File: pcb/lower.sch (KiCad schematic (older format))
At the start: 42 parts, among them J1 MALE, J10 TC2030_NL, J11 STANDOFF, J12 STANDOFF, J13 STANDOFF, J14 STANDOFF, J2 FEMALE, J3 MALE, J4 FEMALE, J5 MALE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

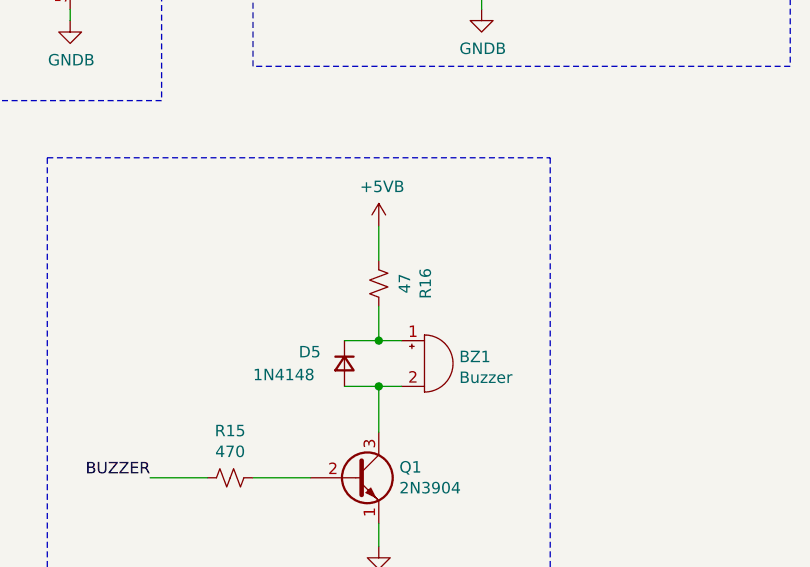
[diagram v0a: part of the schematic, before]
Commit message: Optimize resistor
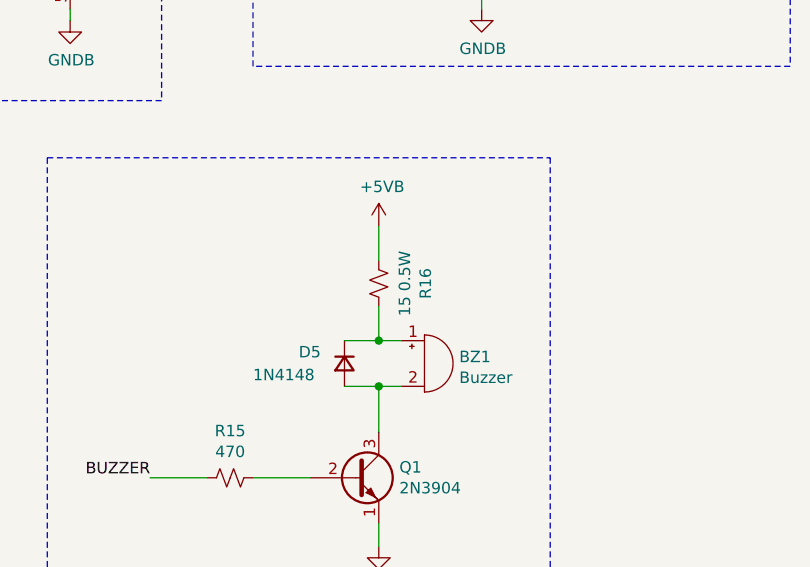
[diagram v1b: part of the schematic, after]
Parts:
- R16: value 47 -> 15 0.5W; footprint Resistor_SMD:R_0402_1005Metric -> Resistor_SMD:R_2010_5025Metric; LCSC Part # C137973 -> C40361; MPN RC0402FR-0747RL -> 2010W2F150JT4E; Manufacturer YAGEO -> Uniroyal Elec; Package 0402 -> 2010
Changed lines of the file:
@@
 P 8500 4650
 F 0 "R16" V 8295 4650 50  0000 C CNN
-F 1 "47" V 8386 4650 50  0000 C CNN
-F 2 "Resistor_SMD:R_0402_1005Metric" H 8500 4650 50  0001 C CNN
-F 3 "https://datasheet.lcsc.com/szlcsc/1810241332_YAGEO-RC0402FR-0747RL_C137973.pdf" H 8500 4650 50  0001 C CNN
-F 4 "C137973" H 8500 4650 50  0001 C CNN "LCSC Part #"
-F 5 "RC0402FR-0747RL" H 8500 4650 50  0001 C CNN "MPN"
-F 6 "YAGEO" H 8500 4650 50  0001 C CNN "Manufacturer"
-F 7 "0402" H 8500 4650 50  0001 C CNN "Package"
+F 1 "15 0.5W" V 8386 4650 50  0000 C CNN
+F 2 "Resistor_SMD:R_2010_5025Metric" H 8500 4650 50  0001 C CNN
+F 3 "https://datasheet.lcsc.com/szlcsc/Uniroyal-Elec-2010W2F150JT4E_C40361.pdf" H 8500 4650 50  0001 C CNN
+F 4 "C40361" H 8500 4650 50  0001 C CNN "LCSC Part #"
+F 5 "2010W2F150JT4E" H 8500 4650 50  0001 C CNN "MPN"
+F 6 "Uniroyal Elec" H 8500 4650 50  0001 C CNN "Manufacturer"
+F 7 "2010" H 8500 4650 50  0001 C CNN "Package"
 	1    8500 4650
 	-1   0    0    1

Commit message: Fix: Wrong pin order
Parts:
- J1, J3, J5, J7: symbol Connector_Generic:Conn_02x02_Counter_Clockwise -> Connector_Generic:Conn_02x02_Top_Bottom
- J2, J4, J6, J8: symbol Connector_Generic:Conn_02x02_Counter_Clockwise -> Connector_Generic:Conn_02x02_Odd_Even
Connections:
- net +5VB: now also J2.3 (Pin_3), J4.3 (Pin_3), J6.3 (Pin_3), J8.3 (Pin_3); no longer J2.1 (Pin_1), J4.1 (Pin_1), J6.1 (Pin_1), J8.1 (Pin_1)
- net GNDB: now also J2.4 (Pin_4), J4.4 (Pin_4), J6.4 (Pin_4), J8.4 (Pin_4); no longer J2.3 (Pin_3), J4.3 (Pin_3), J6.3 (Pin_3), J8.3 (Pin_3)
- net RX1_RXI: now also J2.2 (Pin_2); no longer J2.4 (Pin_4)
- net RX2: no longer J3.4 (Pin_4), J4.4 (Pin_4)
- net RX3: now also J3.4 (Pin_4), J4.2 (Pin_2), J6.2 (Pin_2); no longer J6.4 (Pin_4)
- net RX4: now also J8.2 (Pin_2); no longer J8.4 (Pin_4)
- net TX1_TXO: now also J2.1 (Pin_1); no longer J2.2 (Pin_2)
- net TX2: no longer J3.2 (Pin_2), J4.2 (Pin_2)
- net TX3: now also J3.2 (Pin_2), J4.1 (Pin_1), J6.1 (Pin_1); no longer J6.2 (Pin_2)
- net TX4: now also J8.1 (Pin_1); no longer J8.2 (Pin_2)
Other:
- note added: "1234 in 3D model: male YBRG, female BGYR"
- note removed: "3D model: RGBY = 1234"
